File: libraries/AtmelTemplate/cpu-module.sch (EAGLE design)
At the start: 10 parts, among them CON1 ICSP-HEADER, IC1 MEGA8-AI, IC2 MAX481CSA, IC3 REG1117

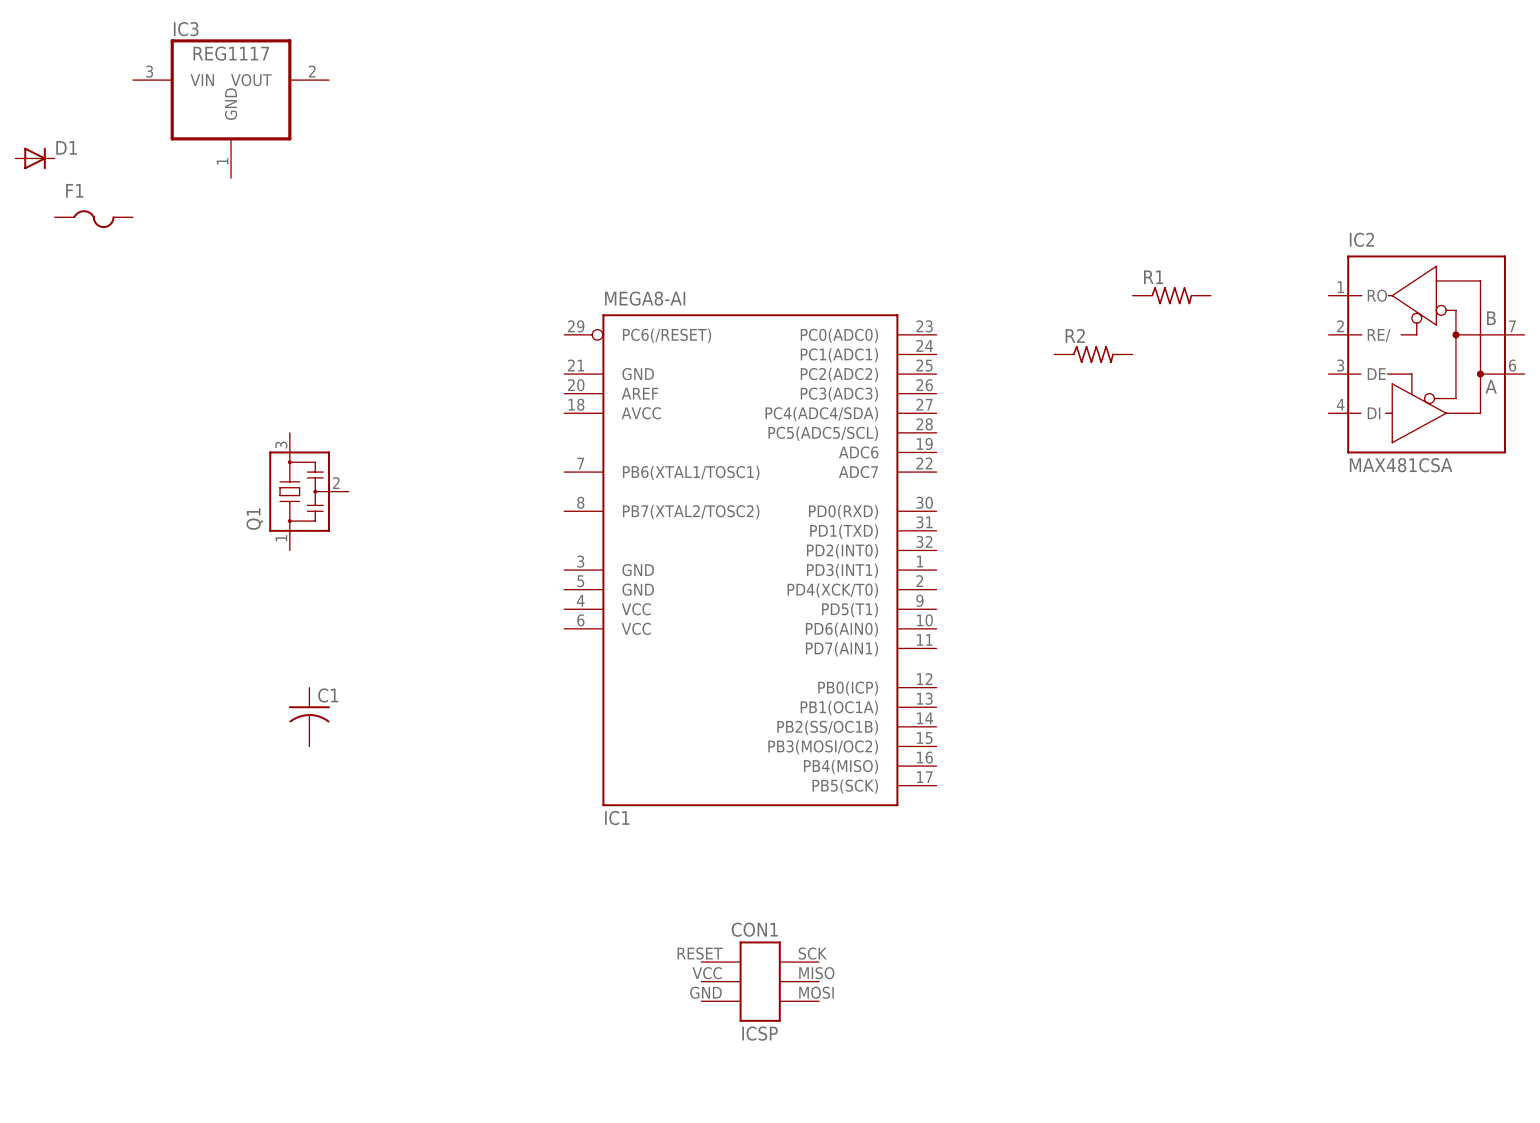
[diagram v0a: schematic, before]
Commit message: Finished schematic of basic Atmel template. Kept all components but microcontroller out, as each board will have its own requirements, plus it would be challenging to keep all pieces from bumping into each other (considering single sided PCB design on both levels)
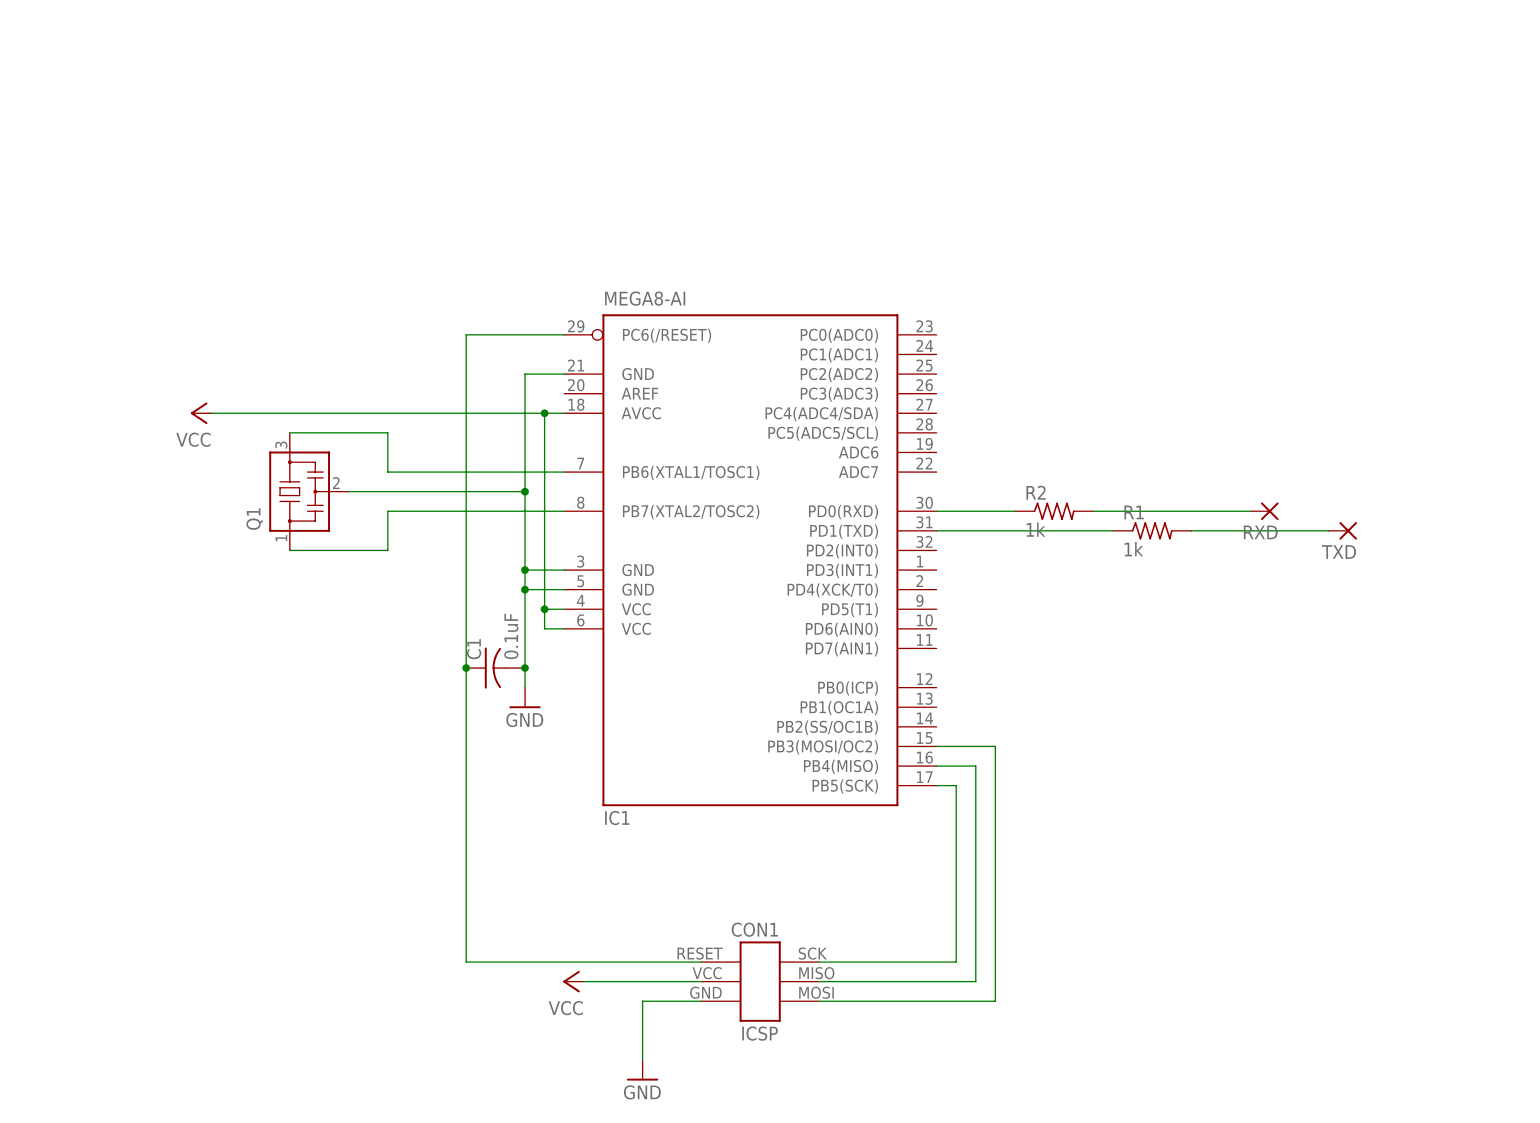
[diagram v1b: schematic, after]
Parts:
- removed D1: (no value), diode:DIODE-MICROMELF-W
- removed F1: (no value), adafruit:PTCFUSE-1812
- removed IC2: MAX481CSA, maxim:MAX481CSA
- removed IC3: REG1117, burr-brown:REG1117
- added RXD, TXD: (no value), wirepad:1,6/0,8
- C1: value (none) -> 0.1uF
- R1, R2: value (none) -> 1k
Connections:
- new net GND: C1.2, CON1.GND, IC1.GND, IC1.GND@1, IC1.GND@2, Q1.2
- new net N$1: IC1.PB6(XTAL1/TOSC1), Q1.3
- new net N$10: R1.2, TXD.P
- new net N$2: IC1.PB7(XTAL2/TOSC2), Q1.1
- new net N$3: C1.1, CON1.RESET, IC1.PC6(/RESET)
- new net N$4: CON1.SCK, IC1.PB5(SCK)
- new net N$5: CON1.MISO, IC1.PB4(MISO)
- new net N$6: CON1.MOSI, IC1.PB3(MOSI/OC2)
- new net N$7: IC1.PD0(RXD), R2.1
- new net N$8: R2.2, RXD.P
- new net N$9: IC1.PD1(TXD), R1.1
- new net VCC: CON1.+5V, IC1.AVCC, IC1.VCC@1, IC1.VCC@2
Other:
- moved on the sheet: C1, R1, R2
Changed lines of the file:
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@@
 <part name="CON1" library="serge" deviceset="ICSP-HEADER" device=""/>
 <part name="Q1" library="serge" deviceset="RESONATOR" device=""/>
-<part name="C1" library="adafruit" deviceset="C-US" device="050-024X044"/>
-<part name="IC2" library="maxim" deviceset="MAX481CSA" device=""/>
-<part name="R1" library="adafruit" deviceset="R-US_" device="R0603"/>
-<part name="R2" library="adafruit" deviceset="R-US_" device="R0603"/>
-<part name="IC3" library="burr-brown" deviceset="REG1117" device=""/>
-<part name="D1" library="diode" deviceset="DIODE-" device="MICROMELF-W"/>
-<part name="F1" library="adafruit" deviceset="PTCFUSE" device="-1812"/>
+<part name="C1" library="adafruit" deviceset="C-US" device="050-024X044" value="0.1uF"/>
+<part name="R1" library="adafruit" deviceset="R-US_" device="R0603" value="1k"/>
+<part name="R2" library="adafruit" deviceset="R-US_" device="R0603" value="1k"/>
+<part name="P+1" library="supply1" deviceset="VCC" device=""/>
+<part name="P+2" library="supply1" deviceset="VCC" device=""/>
+<part name="GND1" library="supply1" deviceset="GND" device=""/>
+<part name="GND2" library="supply1" deviceset="GND" device=""/>
+<part name="RXD" library="wirepad" deviceset="1,6/0,8" device=""/>
+<part name="TXD" library="wirepad" deviceset="1,6/0,8" device=""/>
 </parts>
 <sheets>
@@
 <instance part="CON1" gate="G$1" x="38.1" y="-5.08"/>
 <instance part="Q1" gate="&gt;NAME" x="-22.86" y="58.42" rot="R90"/>
-<instance part="C1" gate="G$1" x="-20.32" y="30.48"/>
-<instance part="IC2" gate="G$1" x="124.46" y="76.2"/>
-<instance part="R1" gate="G$1" x="91.44" y="83.82"/>
-<instance part="R2" gate="G$1" x="81.28" y="76.2"/>
-<instance part="IC3" gate="G$1" x="-30.48" y="111.76"/>
-<instance part="D1" gate="G$1" x="-55.88" y="101.6"/>
-<instance part="F1" gate="G$1" x="-48.26" y="91.44"/>
+<instance part="C1" gate="G$1" x="2.54" y="35.56" rot="R90"/>
+<instance part="R1" gate="G$1" x="88.9" y="53.34"/>
+<instance part="R2" gate="G$1" x="76.2" y="55.88"/>
+<instance part="P+1" gate="VCC" x="12.7" y="-5.08" rot="R90"/>
+<instance part="P+2" gate="VCC" x="-35.56" y="68.58" rot="R90"/>
+<instance part="GND1" gate="1" x="22.86" y="-17.78"/>
+<instance part="GND2" gate="1" x="7.62" y="30.48"/>
+<instance part="RXD" gate="P" x="104.14" y="55.88" rot="R180"/>
+<instance part="TXD" gate="P" x="114.3" y="53.34" rot="R180"/>
 </instances>
 <busses>
 </busses>
 <nets>
+<net name="GND" class="0">
+<segment>
+<pinref part="IC1" gate="G$1" pin="GND@1"/>
+<pinref part="GND2" gate="1" pin="GND"/>
+<wire x1="12.7" y1="48.26" x2="7.62" y2="48.26" width="0.1524" layer="91"/>
+<wire x1="7.62" y1="48.26" x2="7.62" y2="45.72" width="0.1524" layer="91"/>
+<pinref part="IC1" gate="G$1" pin="GND@2"/>
+<wire x1="7.62" y1="45.72" x2="7.62" y2="35.56" width="0.1524" layer="91"/>
+<wire x1="7.62" y1="35.56" x2="7.62" y2="33.02" width="0.1524" layer="91"/>
+<wire x1="12.7" y1="45.72" x2="7.62" y2="45.72" width="0.1524" layer="91"/>
+<junction x="7.62" y="45.72"/>
+<pinref part="IC1" gate="G$1" pin="GND"/>
+<wire x1="12.7" y1="73.66" x2="7.62" y2="73.66" width="0.1524" layer="91"/>
+<wire x1="7.62" y1="73.66" x2="7.62" y2="58.42" width="0.1524" layer="91"/>
+<junction x="7.62" y="48.26"/>
+<pinref part="Q1" gate="&gt;NAME" pin="2"/>
+<wire x1="7.62" y1="58.42" x2="7.62" y2="48.26" width="0.1524" layer="91"/>
+<wire x1="7.62" y1="58.42" x2="-15.24" y2="58.42" width="0.1524" layer="91"/>
+<junction x="7.62" y="58.42"/>
+<pinref part="C1" gate="G$1" pin="2"/>
+<junction x="7.62" y="35.56"/>
+</segment>
+<segment>
+<pinref part="CON1" gate="G$1" pin="GND"/>
+<pinref part="GND1" gate="1" pin="GND"/>
+<wire x1="30.48" y1="-7.62" x2="22.86" y2="-7.62" width="0.1524" layer="91"/>
+<wire x1="22.86" y1="-7.62" x2="22.86" y2="-15.24" width="0.1524" layer="91"/>
+</segment>
+</net>
+<net name="N$1" class="0">
+<segment>
+<pinref part="IC1" gate="G$1" pin="PB6(XTAL1/TOSC1)"/>
+<wire x1="12.7" y1="60.96" x2="-10.16" y2="60.96" width="0.1524" layer="91"/>
+<wire x1="-10.16" y1="60.96" x2="-10.16" y2="66.04" width="0.1524" layer="91"/>
+<pinref part="Q1" gate="&gt;NAME" pin="3"/>
+<wire x1="-10.16" y1="66.04" x2="-22.86" y2="66.04" width="0.1524" layer="91"/>
+</segment>
+</net>
+<net name="N$2" class="0">
+<segment>
+<pinref part="IC1" gate="G$1" pin="PB7(XTAL2/TOSC2)"/>
+<wire x1="12.7" y1="55.88" x2="-10.16" y2="55.88" width="0.1524" layer="91"/>
+<wire x1="-10.16" y1="55.88" x2="-10.16" y2="50.8" width="0.1524" layer="91"/>
+<pinref part="Q1" gate="&gt;NAME" pin="1"/>
+<wire x1="-10.16" y1="50.8" x2="-22.86" y2="50.8" width="0.1524" layer="91"/>
+</segment>
+</net>
+<net name="VCC" class="0">
+<segment>
+<pinref part="IC1" gate="G$1" pin="AVCC"/>
+<pinref part="P+2" gate="VCC" pin="VCC"/>
+<wire x1="12.7" y1="68.58" x2="10.16" y2="68.58" width="0.1524" layer="91"/>
+<pinref part="IC1" gate="G$1" pin="VCC@1"/>
+<wire x1="10.16" y1="68.58" x2="-33.02" y2="68.58" width="0.1524" layer="91"/>
+<wire x1="12.7" y1="43.18" x2="10.16" y2="43.18" width="0.1524" layer="91"/>
+<wire x1="10.16" y1="43.18" x2="10.16" y2="68.58" width="0.1524" layer="91"/>
+<junction x="10.16" y="68.58"/>
+<pinref part="IC1" gate="G$1" pin="VCC@2"/>
+<wire x1="12.7" y1="40.64" x2="10.16" y2="40.64" width="0.1524" layer="91"/>
+<wire x1="10.16" y1="40.64" x2="10.16" y2="43.18" width="0.1524" layer="91"/>
+<junction x="10.16" y="43.18"/>
+</segment>
+<segment>
+<pinref part="CON1" gate="G$1" pin="+5V"/>
+<pinref part="P+1" gate="VCC" pin="VCC"/>
+<wire x1="30.48" y1="-5.08" x2="15.24" y2="-5.08" width="0.1524" layer="91"/>
+</segment>
+</net>
+<net name="N$3" class="0">
+<segment>
+<pinref part="CON1" gate="G$1" pin="RESET"/>
+<wire x1="30.48" y1="-2.54" x2="0" y2="-2.54" width="0.1524" layer="91"/>
+<wire x1="0" y1="-2.54" x2="0" y2="35.56" width="0.1524" layer="91"/>
+<pinref part="IC1" gate="G$1" pin="PC6(/RESET)"/>
+<wire x1="0" y1="35.56" x2="0" y2="78.74" width="0.1524" layer="91"/>
+<wire x1="0" y1="78.74" x2="12.7" y2="78.74" width="0.1524" layer="91"/>
+<pinref part="C1" gate="G$1" pin="1"/>
+<junction x="0" y="35.56"/>
+</segment>
+</net>
+<net name="N$4" class="0">
+<segment>
+<pinref part="CON1" gate="G$1" pin="SCK"/>
+<wire x1="45.72" y1="-2.54" x2="63.5" y2="-2.54" width="0.1524" layer="91"/>
+<wire x1="63.5" y1="-2.54" x2="63.5" y2="20.32" width="0.1524" layer="91"/>
+<pinref part="IC1" gate="G$1" pin="PB5(SCK)"/>
+<wire x1="63.5" y1="20.32" x2="60.96" y2="20.32" width="0.1524" layer="91"/>
+</segment>
+</net>
+<net name="N$5" class="0">
+<segment>
+<pinref part="IC1" gate="G$1" pin="PB4(MISO)"/>
+<wire x1="60.96" y1="22.86" x2="66.04" y2="22.86" width="0.1524" layer="91"/>
+<wire x1="66.04" y1="22.86" x2="66.04" y2="-5.08" width="0.1524" layer="91"/>
+<pinref part="CON1" gate="G$1" pin="MISO"/>
+<wire x1="66.04" y1="-5.08" x2="45.72" y2="-5.08" width="0.1524" layer="91"/>
+</segment>
+</net>
+<net name="N$6" class="0">
+<segment>
+<pinref part="CON1" gate="G$1" pin="MOSI"/>
+<wire x1="45.72" y1="-7.62" x2="68.58" y2="-7.62" width="0.1524" layer="91"/>
+<wire x1="68.58" y1="-7.62" x2="68.58" y2="25.4" width="0.1524" layer="91"/>
+<pinref part="IC1" gate="G$1" pin="PB3(MOSI/OC2)"/>
+<wire x1="68.58" y1="25.4" x2="60.96" y2="25.4" width="0.1524" layer="91"/>
+</segment>
+</net>
+<net name="N$7" class="0">
+<segment>
+<pinref part="IC1" gate="G$1" pin="PD0(RXD)"/>
+<pinref part="R2" gate="G$1" pin="1"/>
+<wire x1="60.96" y1="55.88" x2="71.12" y2="55.88" width="0.1524" layer="91"/>
+</segment>
+</net>
+<net name="N$8" class="0">
+<segment>
+<pinref part="R2" gate="G$1" pin="2"/>
+<pinref part="RXD" gate="P" pin="P"/>
+<wire x1="81.28" y1="55.88" x2="101.6" y2="55.88" width="0.1524" layer="91"/>
+</segment>
+</net>
+<net name="N$9" class="0">
+<segment>
+<pinref part="IC1" gate="G$1" pin="PD1(TXD)"/>
+<pinref part="R1" gate="G$1" pin="1"/>
+<wire x1="60.96" y1="53.34" x2="83.82" y2="53.34" width="0.1524" layer="91"/>
+</segment>
+</net>
+<net name="N$10" class="0">
+<segment>
+<pinref part="R1" gate="G$1" pin="2"/>
+<pinref part="TXD" gate="P" pin="P"/>
+<wire x1="93.98" y1="53.34" x2="111.76" y2="53.34" width="0.1524" layer="91"/>
+</segment>
+</net>
 </nets>
 </sheet>

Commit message: v1 of CPU module board finished
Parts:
- removed Q1: (no value), serge:RESONATOR
- removed RXD, TXD: (no value), wirepad:1,6/0,8
- added C2, C3: 18pF, adafruit:C-USC0805
- added C4: 100nF, adafruit:C-USC0603K
- added JP1: (no value), adafruit:PINHD-1X6B
- added JP2: (no value), adafruit:PINHD-1X8BIG
- added Q2: CSM-7X-DU, crystal:CSM-7X-DU
- C1: value 0.1uF -> 100nF; device adafruit:C-US050-024X044 -> adafruit:C-USC0603K
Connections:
- new net N$11: IC1.PC1(ADC1), JP2.1
- new net N$12: CON1.RESET, IC1.PC6(/RESET)
- new net N$13: IC1.PC2(ADC2), JP2.2
- new net N$14: IC1.PC3(ADC3), JP2.3
- new net N$15: IC1.PC4(ADC4/SDA), JP2.4
- new net N$16: IC1.PC5(ADC5/SCL), JP2.5
- new net N$17: IC1.PB2(SS/OC1B), JP1.6
- new net N$18: IC1.PB1(OC1A), JP1.5
- new net N$19: IC1.PB0(ICP), JP1.4
- new net N$20: IC1.PD7(AIN1), JP1.3
- new net N$21: IC1.PD6(AIN0), JP1.2
- new net N$22: IC1.PD5(T1), JP1.1
- new net N$23: JP2.6, R2.2
- net GND: now also C2.2, C3.2, C4.1; no longer Q1.2
- net N$1: now also C2.1, Q2.2; no longer Q1.3
- net N$10: now also IC1.PD2(INT0), JP2.8; no longer R1.2, TXD.P
- net N$2: now also C3.1, Q2.1; no longer Q1.1
- net N$3: now also C4.2, IC1.AREF; no longer C1.1, CON1.RESET, IC1.PC6(/RESET)
- net N$8: now also JP2.7, R1.2; no longer R2.2, RXD.P
- net VCC: now also C1.1
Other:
- moved on the sheet: C1, R1, R2
